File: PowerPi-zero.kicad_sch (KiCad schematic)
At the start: 52 parts, among them IC2 TPS51397ARJER, J1 2444, J2 JST XH 01x02, J6 Raspberry_Pi_2_3, J8 JST XH 01x02, Q1 SiA471DJ, Q2 SiA430DJT, U1 LM74700

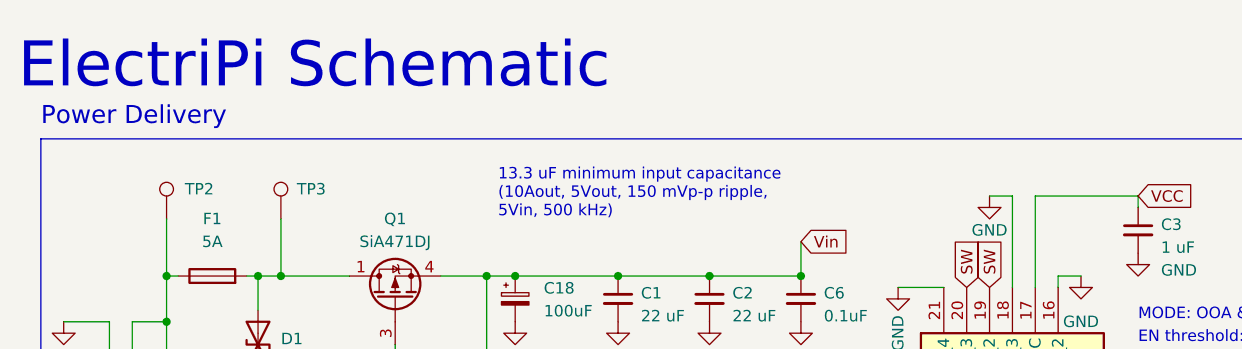
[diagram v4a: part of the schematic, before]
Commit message: silk fixed, DRC and DFM changes
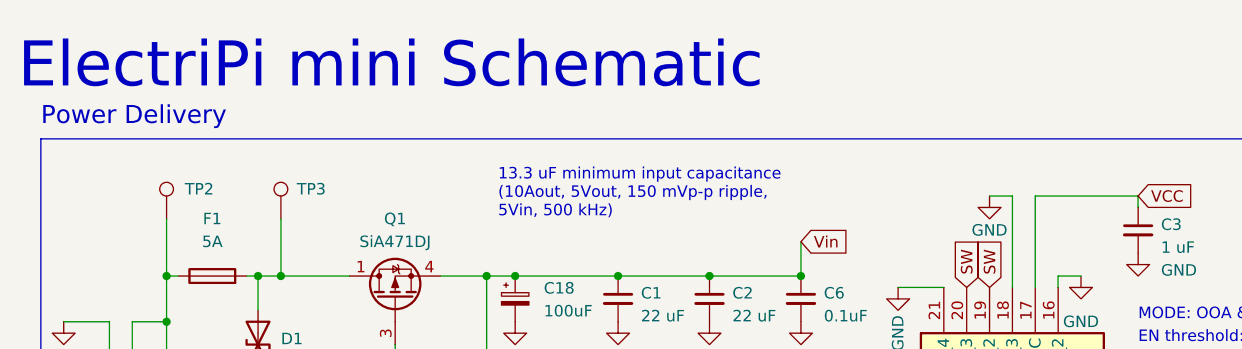
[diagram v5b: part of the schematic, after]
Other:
- note added: "ElectriPi mini Schematic"
- note removed: "ElectriPi Schematic"
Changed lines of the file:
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@@
     (effects (font (size 1.27 1.27)) (justify left bottom))
   )
-  (text "ElectriPi Schematic" (at 15.24 20.32 0)
+  (text "ElectriPi mini Schematic" (at 15.24 20.32 0)
     (effects (font (size 5 5)) (justify left bottom))
   )
